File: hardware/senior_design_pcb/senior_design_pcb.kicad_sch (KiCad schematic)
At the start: 0 parts

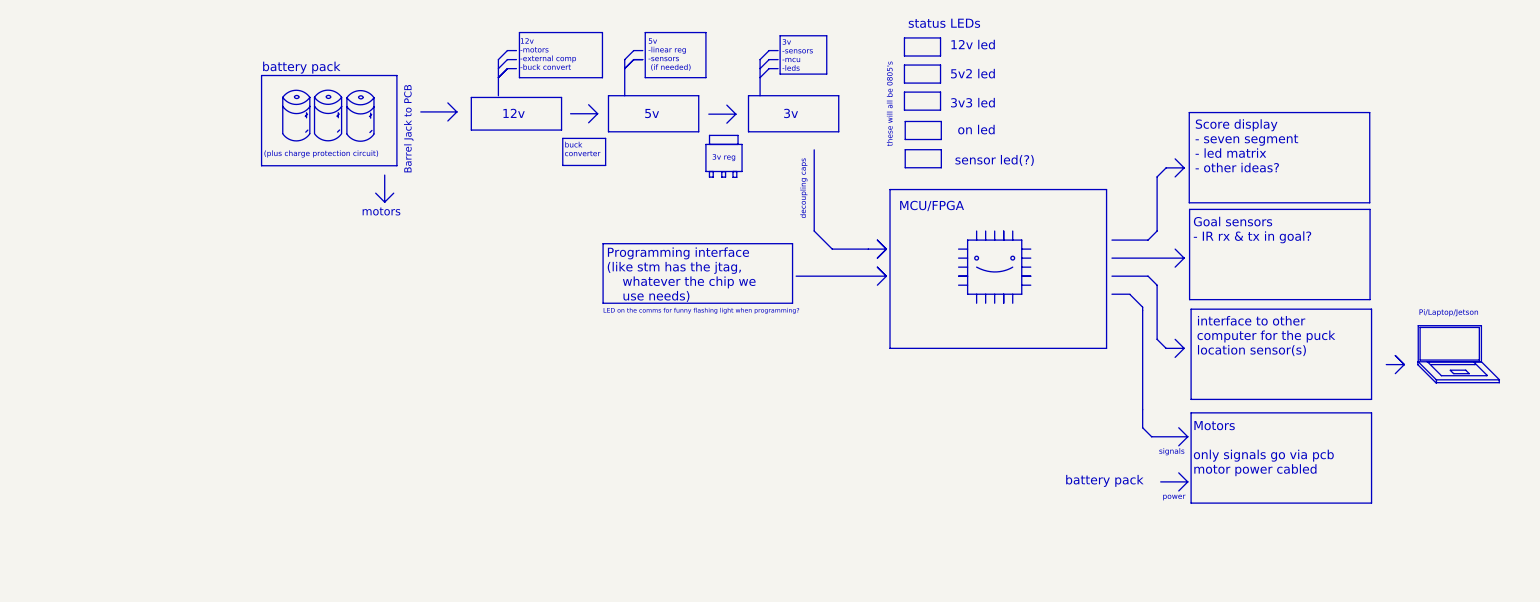
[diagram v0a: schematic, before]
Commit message: began schematic
made a subsheet with components on it. referencing ece362 dev board and my own work. basic stuff so far for just powering and programming the stm
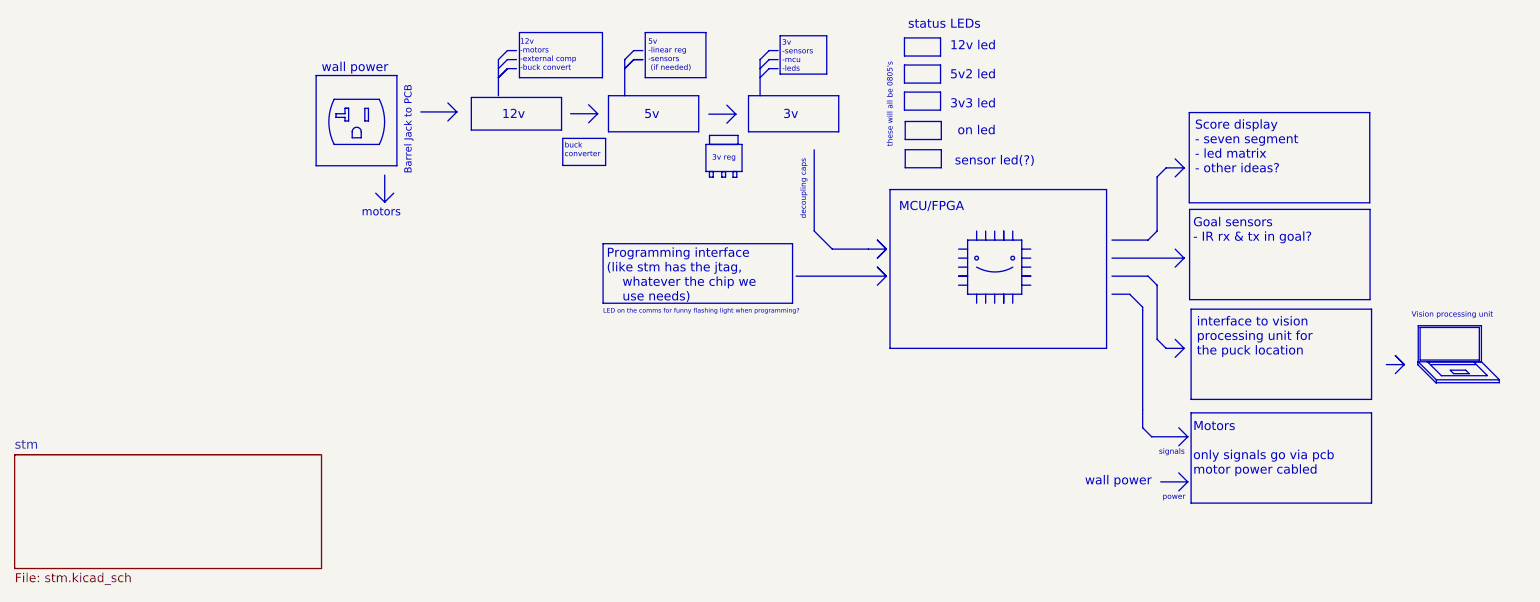
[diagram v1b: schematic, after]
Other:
- added sheet stm (stm.kicad_sch)
- note added: "Vision processing unit"
- note added: "interface to vision processing unit for the puck location"
- note added: "wall power"
- note removed: "(plus charge protection circuit)"
- note removed: "Pi/Laptop/Jetson"
- note removed: "battery pack"
- note removed: "interface to other computer for the puck location sensor(s)"
- title: (none) -> AutonAir STM

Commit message: pushing for the night
minor updates including adding more words and realigning things
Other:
- note added: "STM"
- note added: "connection to buck conv and motors"
- note added: "from JTAG"
- note added: "not on pcb"
- note added: "will be powered by laptop"
- note removed: "Barrel Jack to PCB"
- note removed: "MCU/FPGA"

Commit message: moved some stuff
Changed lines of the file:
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@@
 	)
 	(sheet
-		(at 17.78 99.06)
+		(at 26.924 104.648)
 		(size 43.18 16.002)
 		(exclude_from_sim no)
@@
 		)
 		(property "Sheetname" "stm"
-			(at 17.78 98.3484 0)
+			(at 26.924 103.9364 0)
 			(effects
 				(font
@@
 		)
 		(property "Sheetfile" "stm.kicad_sch"
-			(at 17.78 115.6466 0)
+			(at 26.924 121.2346 0)
 			(effects
 				(font

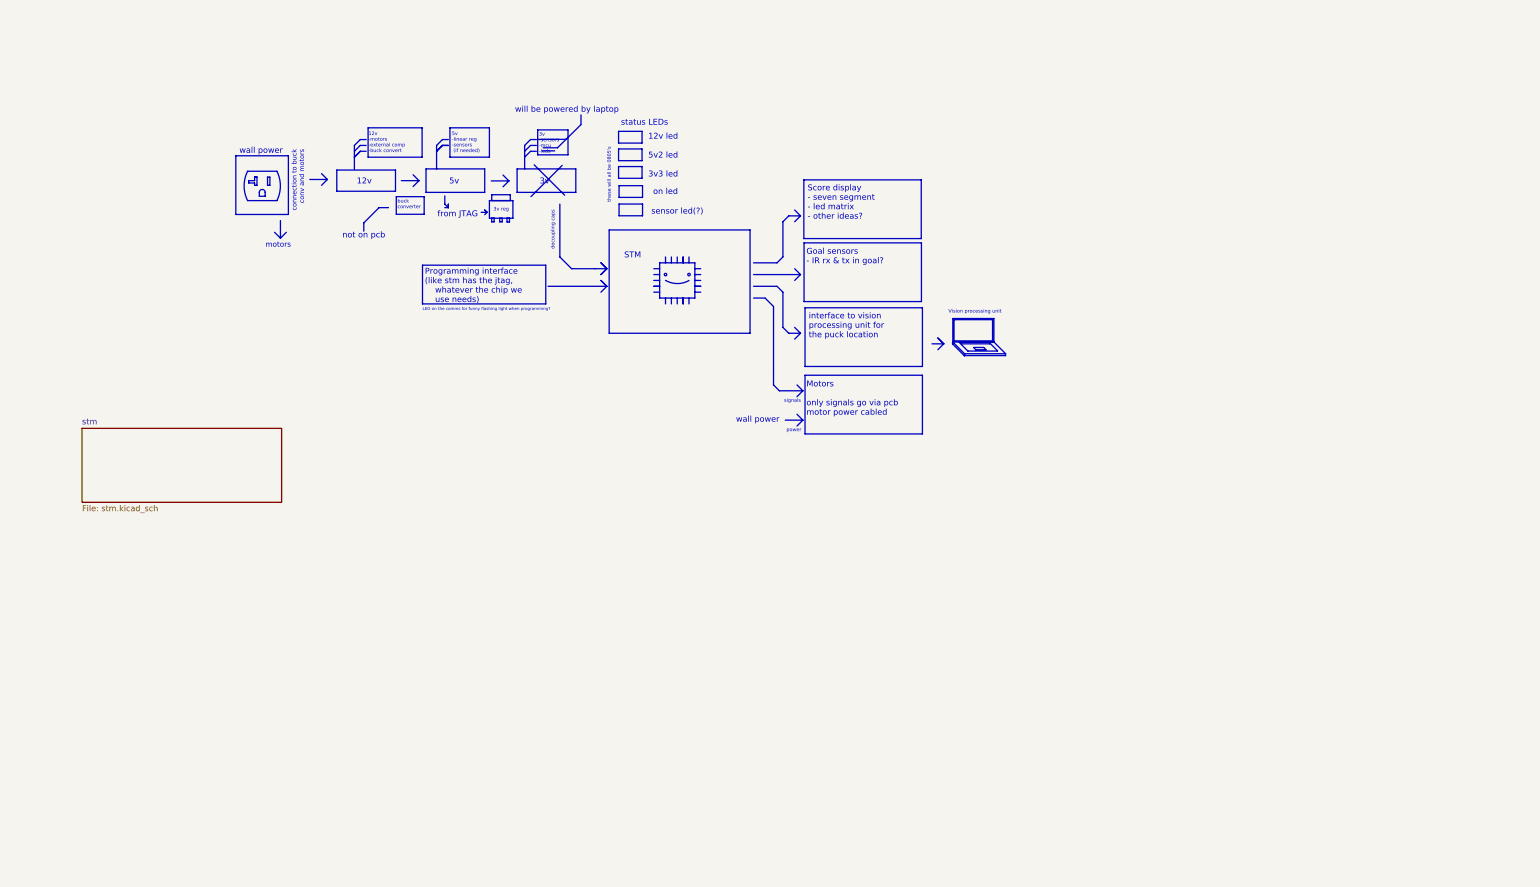
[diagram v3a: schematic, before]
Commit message: added pcb, removed schematic level
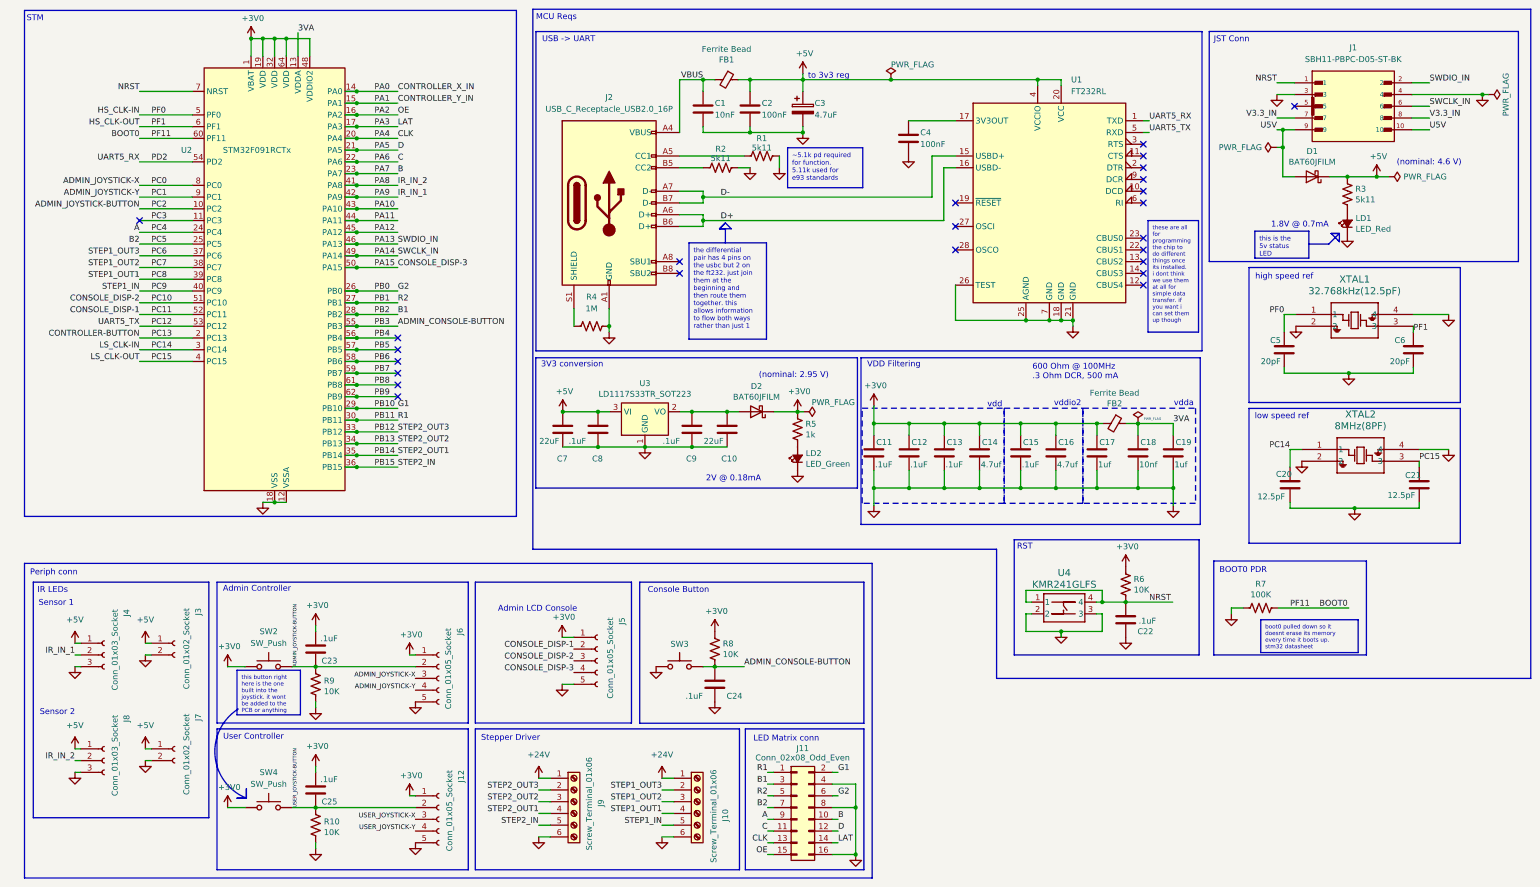
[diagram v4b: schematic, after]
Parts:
- added C1: 10nF, Capacitor_SMD:C_0805_2012Metric_Pad1.18x1.45mm_HandSolder, symbol Device:C
- added C10, C7: 22uF, Capacitor_SMD:C_0805_2012Metric_Pad1.18x1.45mm_HandSolder, symbol Device:C
- added C11, C12, C13, C15, C22, C23, C24, C25, C8, C9: .1uF, Capacitor_SMD:C_0805_2012Metric_Pad1.18x1.45mm_HandSolder, symbol Device:C
- added C14, C16: 4.7uf, Capacitor_SMD:C_0805_2012Metric_Pad1.18x1.45mm_HandSolder, symbol Device:C
- added C17, C19: 1uf, Capacitor_SMD:C_0805_2012Metric_Pad1.18x1.45mm_HandSolder, symbol Device:C
- added C18: 10nf, Capacitor_SMD:C_0805_2012Metric_Pad1.18x1.45mm_HandSolder, symbol Device:C
- added C2, C4: 100nF, Capacitor_SMD:C_0805_2012Metric_Pad1.18x1.45mm_HandSolder, symbol Device:C
- added C20, C21: 12.5pF, Capacitor_SMD:C_0805_2012Metric_Pad1.18x1.45mm_HandSolder, symbol Device:C
- added C3: 4.7uF, Capacitor_SMD:C_0805_2012Metric_Pad1.18x1.45mm_HandSolder, symbol Device:C_Polarized
- added C5, C6: 20pF, Capacitor_SMD:C_0805_2012Metric_Pad1.18x1.45mm_HandSolder, symbol Device:C
- added D1, D2: BAT60JFILM, Diode_SMD:D_SOD-323_HandSoldering, symbol Diode:BAT60A
- added FB1, FB2: Ferrite Bead, Inductor_SMD:L_0805_2012Metric_Pad1.05x1.20mm_HandSolder, symbol Device:Ferrite_Bead_Small
- added J1: SBH11-PBPC-D05-ST-BK, General Library:jtag_conn, symbol jtag_conn:SBH11-PBPC-D05-ST-BK
- added J10, J9: Screw_Terminal_01x06, Connector_JST:JST_EH_S6B-EH_1x06_P2.50mm_Horizontal, symbol Connector:Screw_Terminal_01x06
- added J11: Conn_02x08_Odd_Even, Connector_PinSocket_2.54mm:PinSocket_2x08_P2.54mm_Vertical, symbol Connector_Generic:Conn_02x08_Odd_Even
- added J12, J5, J6: Conn_01x05_Socket, Connector_JST:JST_EH_S5B-EH_1x05_P2.50mm_Horizontal, symbol Connector:Conn_01x05_Socket
- added J2: USB_C_Receptacle_USB2.0_16P, Sr_ Design:USB-C-PORT-2, symbol Connector:USB_C_Receptacle_USB2.0_16P
- added J3, J7: Conn_01x02_Socket, Connector_JST:JST_EH_S2B-EH_1x02_P2.50mm_Horizontal, symbol Connector:Conn_01x02_Socket
- added J4, J8: Conn_01x03_Socket, Connector_JST:JST_EH_S3B-EH_1x03_P2.50mm_Horizontal, symbol Connector:Conn_01x03_Socket
- added LD1: LED_Red, LED_SMD:LED_0805_2012Metric, symbol Device:LED_Small_ALT
- added LD2: LED_Green, LED_SMD:LED_0805_2012Metric, symbol Device:LED_Small_ALT
- added R1, R2, R3: 5k11, Resistor_SMD:R_0805_2012Metric_Pad1.20x1.40mm_HandSolder, symbol Device:R_US
- added R10, R6, R8, R9: 10K, Resistor_SMD:R_0805_2012Metric_Pad1.20x1.40mm_HandSolder, symbol Device:R_US
- added R4: 1M, Resistor_SMD:R_0805_2012Metric_Pad1.20x1.40mm_HandSolder, symbol Device:R_US
- added R5: 1k, Resistor_SMD:R_0805_2012Metric_Pad1.20x1.40mm_HandSolder, symbol Device:R_US
- added R7: 100K, Resistor_SMD:R_0805_2012Metric_Pad1.20x1.40mm_HandSolder, symbol Device:R_US
- added SW2, SW4: SW_Push, symbol Switch:SW_Push
- added SW3: SW_Push, Connector_PinHeader_2.54mm:PinHeader_1x02_P2.54mm_Vertical, symbol Switch:SW_Push
- added U1: FT232RL, Package_SO:SSOP-28_5.3x10.2mm_P0.65mm, symbol Interface_USB:FT232RL
- added U2: STM32F091RCTx, Package_QFP:LQFP-64_10x10mm_P0.5mm, symbol MCU_ST_STM32F0:STM32F091RCTx
- added U3: LD1117S33TR_SOT223, Package_TO_SOT_SMD:SOT-223-3_TabPin2, symbol Regulator_Linear:LD1117S33TR_SOT223
- added U4: KMR241GLFS, General Library:KMR241G-RESET-BUTTON, symbol KMR241G-RESET-BUTTON:KMR241GLFS
- added XTAL1: 32.768kHz(12.5pF), Sr_ Design:ECS - CRYSTAL 32.7680KHZ 6PF SMD, symbol ECS-CRYSTAL 8MHZ 8PF SMD:ECS-80-8-33Q-ADS
- added XTAL2: 8MHz(8PF), Sr_ Design:ECS-CRYSTAL 8MHZ 8PF SMD, symbol ECS-CRYSTAL 8MHZ 8PF SMD:ECS-80-8-33Q-ADS
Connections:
- new net: C10.1, C9.1, D2.2 (A), U3.2 (VO)
- new net: LD1.2 (A), R3.2
- new net: LD2.2 (A), R5.2
- new net: C4.1, U1.17 (3V3OUT)
- new net: J2.A5 (CC1), R1.1
- new net: J2.B5 (CC2), R2.1
- new net: J2.S1 (SHIELD), R4.1
- new net +24V: J10.1 (Pin_1), J9.1 (Pin_1)
- new net +3V0: C11.1, C12.1, C13.1, C14.1, C15.1, C16.1, C17.1, C23.1, C25.1, D2.1 (K), FB2.2, J12.1 (Pin_1), J5.1 (Pin_1), J6.1 (Pin_1), R5.1, R6.1, R8.1, SW2.1, SW4.1, U2.1 (VBAT), U2.19 (VDD), U2.32 (VDD), U2.48 (VDDIO2), U2.64 (VDD)
- new net +5V: C2.1, C3.1, C7.1, C8.1, D1.1 (K), FB1.1, J3.1 (Pin_1), J4.1 (Pin_1), J7.1 (Pin_1), J8.1 (Pin_1), R3.1, U1.20 (VCC), U1.4 (VCCIO), U3.3 (VI)
- new net 3VA: C18.1, C19.1, FB2.1, U2.13 (VDDA)
- new net A: J11.9 (Pin_9), U2.24 (PC4)
- new net ADMIN_CONSOLE-BUTTON: C24.1, R8.2, SW3.2, U2.55 (PB3)
- new net ADMIN_JOYSTICK-BUTTON: C23.2, J6.2 (Pin_2), R9.1, SW2.2, U2.10 (PC2)
- new net ADMIN_JOYSTICK-X: J6.3 (Pin_3), U2.8 (PC0)
- new net ADMIN_JOYSTICK-Y: J6.4 (Pin_4), U2.9 (PC1)
- new net B: J11.10 (Pin_10), U2.23 (PA7)
- new net B1: J11.3 (Pin_3), U2.28 (PB2)
- new net B2: J11.7 (Pin_7), U2.25 (PC5)
- new net BOOT0: R7.1, U2.60 (PF11)
- new net C: J11.11 (Pin_11), U2.22 (PA6)
- new net CLK: J11.13 (Pin_13), U2.20 (PA4)
- new net CONSOLE_DISP-1: J5.2 (Pin_2), U2.52 (PC11)
- new net CONSOLE_DISP-2: J5.3 (Pin_3), U2.51 (PC10)
- new net CONSOLE_DISP-3: J5.4 (Pin_4), U2.50 (PA15)
- new net CONTROLLER-BUTTON: U2.2 (PC13)
- new net CONTROLLER_X_IN: U2.14 (PA0)
- new net CONTROLLER_Y_IN: U2.15 (PA1)
- new net D: J11.12 (Pin_12), U2.21 (PA5)
- new net D+: J2.A6 (D+), J2.B6 (D+), U1.16 (USBD-)
- new net D-: J2.A7 (D-), J2.B7 (D-), U1.15 (USBD+)
- new net G1: J11.2 (Pin_2), U2.29 (PB10)
- new net G2: J11.6 (Pin_6), U2.26 (PB0)
- new net GND: C1.2, C10.2, C11.2, C12.2, C13.2, C14.2, C15.2, C16.2, C17.2, C18.2, C19.2, C2.2, C20.2, C21.2, C22.2, C24.2, C3.2, C4.2, C5.2, C6.2, C7.2, C8.2, C9.2, J1.3, J1.4, J10.6 (Pin_6), J11.16 (Pin_16), J11.4 (Pin_4), J11.8 (Pin_8), J12.5 (Pin_5), J2.A1 (GND), J2.A12 (GND), J2.B1 (GND), J2.B12 (GND), J3.2 (Pin_2), J4.3 (Pin_3), J5.5 (Pin_5), J6.5 (Pin_5), J7.2 (Pin_2), J8.3 (Pin_3), J9.6 (Pin_6), LD1.1 (K), LD2.1 (K), R1.2, R10.2, R2.2, R4.2, R7.2, R9.2, SW3.1, U1.18 (GND), U1.21 (GND), U1.25 (AGND), U1.26 (TEST), U1.7 (GND), U2.12 (VSSA), U2.18 (VSS), U2.31 (VSS), U2.47 (VSS), U2.63 (VSS), U3.1 (GND), U4.2, U4.3, XTAL1.2, XTAL1.4, XTAL2.2, XTAL2.4
- new net HS_CLK-IN: C5.1, U2.5 (PF0), XTAL1.1
- new net HS_CLK-OUT: C6.1, U2.6 (PF1), XTAL1.3
- new net IR_IN_1: J4.2 (Pin_2), U2.42 (PA9)
- new net IR_IN_2: J8.2 (Pin_2), U2.41 (PA8)
- new net LAT: J11.14 (Pin_14), U2.17 (PA3)
- new net LS_CLK-IN: C20.1, U2.3 (PC14), XTAL2.1
- new net LS_CLK-OUT: C21.1, U2.4 (PC15), XTAL2.3
- new net NRST: C22.1, J1.1, R6.2, U2.7 (NRST), U4.1, U4.4
- new net OE: J11.15 (Pin_15), U2.16 (PA2)
- new net PA10: U2.43 (PA10)
- new net PA11: U2.44 (PA11)
- new net PA12: U2.45 (PA12)
- new net PA13: J1.2, U2.46 (PA13)
- new net PA14: J1.6, U2.49 (PA14)
- new net PB1: J11.5 (Pin_5), U2.27 (PB1)
- new net PB11: J11.1 (Pin_1), U2.30 (PB11)
- new net PB12: J9.2 (Pin_2), U2.33 (PB12)
- new net PB13: J9.3 (Pin_3), U2.34 (PB13)
- new net PB14: J9.4 (Pin_4), U2.35 (PB14)
- new net PB15: J9.5 (Pin_5), U2.36 (PB15)
- new net PB4: U2.56 (PB4)
- new net PB5: U2.57 (PB5)
- new net PB6: U2.58 (PB6)
- new net PB7: U2.59 (PB7)
- new net PB8: U2.61 (PB8)
- new net PB9: U2.62 (PB9)
- new net PC12: U1.5 (RXD), U2.53 (PC12)
- new net PC3: U2.11 (PC3)
- new net PC6: J10.2 (Pin_2), U2.37 (PC6)
- new net PC7: J10.3 (Pin_3), U2.38 (PC7)
- new net PC8: J10.4 (Pin_4), U2.39 (PC8)
- new net PC9: J10.5 (Pin_5), U2.40 (PC9)
- new net PD2: U1.1 (TXD), U2.54 (PD2)
- new net U5V: D1.2 (A), J1.10, J1.9
- new net USER_JOYSTICK-BUTTON: C25.2, J12.2 (Pin_2), R10.1, SW4.2
- new net USER_JOYSTICK-X: J12.3 (Pin_3)
- new net USER_JOYSTICK-Y: J12.4 (Pin_4)
- new net V3.3_IN: J1.7, J1.8
- new net VBUS: C1.1, FB1.2, J2.A4 (VBUS), J2.A9 (VBUS), J2.B4 (VBUS), J2.B9 (VBUS)
- no-connect marks 0 -> 24
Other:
- removed sheet stm
- note added: "(nominal: 2.95 V)"
- note added: "(nominal: 4.6 V)"
- note added: "1.8V @ 0.7mA"
- note added: "2V @ 0.18mA"
- note added: "3V3 conversion"
- note added: "600 Ohm @ 100MHz .3 Ohm DCR, 500 mA"
- note added: "Admin Controller"
- note added: "Admin LCD Console"
- note added: "BOOT0 PDR"
- note added: "Console Button"
- note added: "IR LEDs"
- note added: "JST Conn"
- note added: "LED Matrix conn"
- note added: "MCU Reqs"
- note added: "Periph conn"
- note added: "RST"
- note added: "Sensor 1"
- note added: "Sensor 2"
- note added: "Stepper Driver"
- note added: "USB -> UART"
- note added: "User Controller"
- note added: "VDD Filtering"
- note added: "high speed ref"
- note added: "low speed ref"
- note added: "to 3v3 reg"
- note added: "vdd"
- note added: "vdda"
- note added: "vddio2"
- note removed: "12v"
- note removed: "12v -motors -external comp -buck convert"
- note removed: "12v led 5v2 led 3v3 led"
- note removed: "3v"
- note removed: "3v -sensors -mcu -leds"
- note removed: "3v reg"
- note removed: "5v"
- note removed: "5v -linear reg -sensors (if needed)"
- note removed: "Goal sensors - IR rx & tx in goal?"
- note removed: "LED on the comms for funny flashing light when programming?"
- note removed: "Motors only signals go via pcb motor power cabled"
- note removed: "Programming interface (like stm has the jtag, whatever the chip we use needs)"
- note removed: "Score display - seven segment - led matrix - other ideas?"
- note removed: "Vision processing unit"
- note removed: "buck converter"
- note removed: "connection to buck conv and motors"
- note removed: "decoupling caps"
- note removed: "from JTAG"
- note removed: "interface to vision processing unit for the puck location"
- note removed: "motors"
- note removed: "not on pcb"
- note removed: "on led"
- note removed: "power"
- note removed: "sensor led(?)"
- note removed: "signals"
- note removed: "status LEDs"
- note removed: "these will all be 0805's"
- note removed: "wall power"
- note removed: "will be powered by laptop"
